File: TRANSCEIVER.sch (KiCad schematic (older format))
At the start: 9 parts

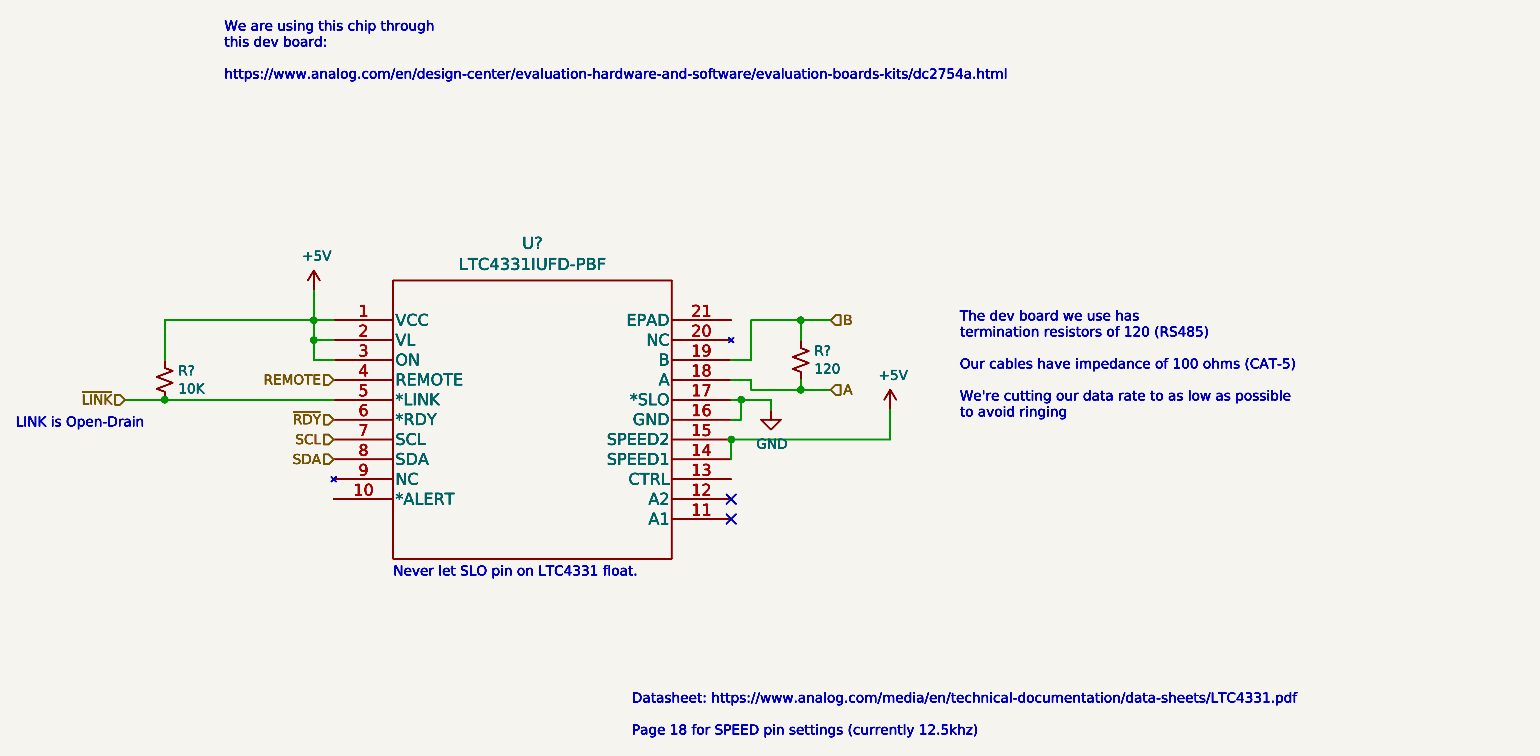
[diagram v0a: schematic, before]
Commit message: Got rid of overlying duplicate parts
Some identical parts were placed over eachother which showed up when annotating references
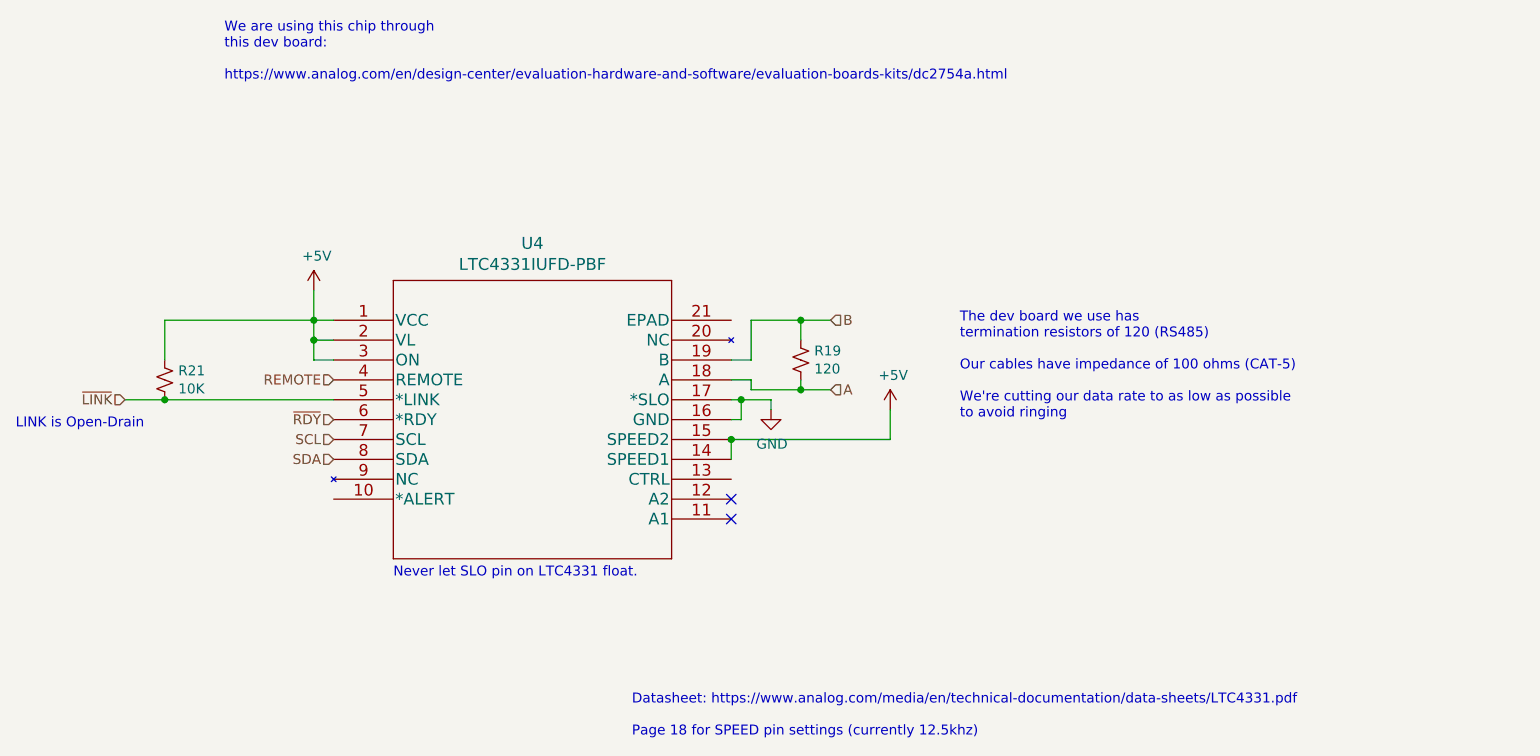
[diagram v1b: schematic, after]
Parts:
- removed R? (x2): 120, symbol Device:R_Small_US
- removed R? (x2): 10K, symbol Device:R_Small_US
- removed U? (x2): LTC4331IUFD-PBF, QFN_20_ADI, symbol 2020-09-01_04-44-37:LTC4331IUFD-PBF
- gave numbers to parts that had none: 3
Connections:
- no-connect marks 6 -> 2
